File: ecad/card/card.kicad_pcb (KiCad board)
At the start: 4 copper layers, 133.4 x 32.2 mm, 136 parts, among them J1 Conn_01x03_Pin, J2 USB4105-GF-A, J3 10145226-0241N13LF, J4 Conn_01x03_Pin, J5 Conn_01x03_Pin, SW1 SW_Push, SW2 SW_Push, U1 W25Q128JVS, U2 RP2350_80QFN, U3 MCP23017_SO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

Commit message: current production try
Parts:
- SW1, SW2: footprint Button_Switch_SMD:SW_Push_1P1T_NO_Vertical_Wuerth_434133025816 -> Library:SW_TS-1088-AR02016
- turned SW1 to 180 degrees
- turned SW2 to 180 degrees
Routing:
- net /~{USB_BOOT}: track 7.50 -> 2.23 mm
- net GND: track 212.7 -> 207.6 mm, vias 52 -> 51
- net Net-(R1-Pad2): track 5.62 -> 1.90 mm
- net /~{RESET}: track 127.2 -> 128.4 mm

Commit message: revisions after feedback
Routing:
- net GND: track 207.6 -> 208.3 mm

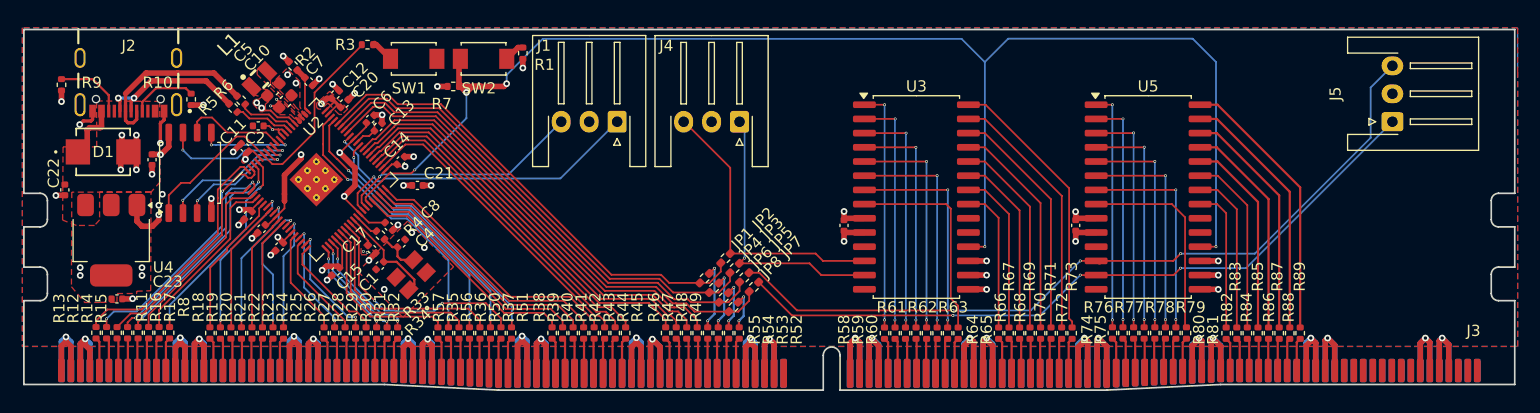
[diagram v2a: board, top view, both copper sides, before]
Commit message: various production cost changes
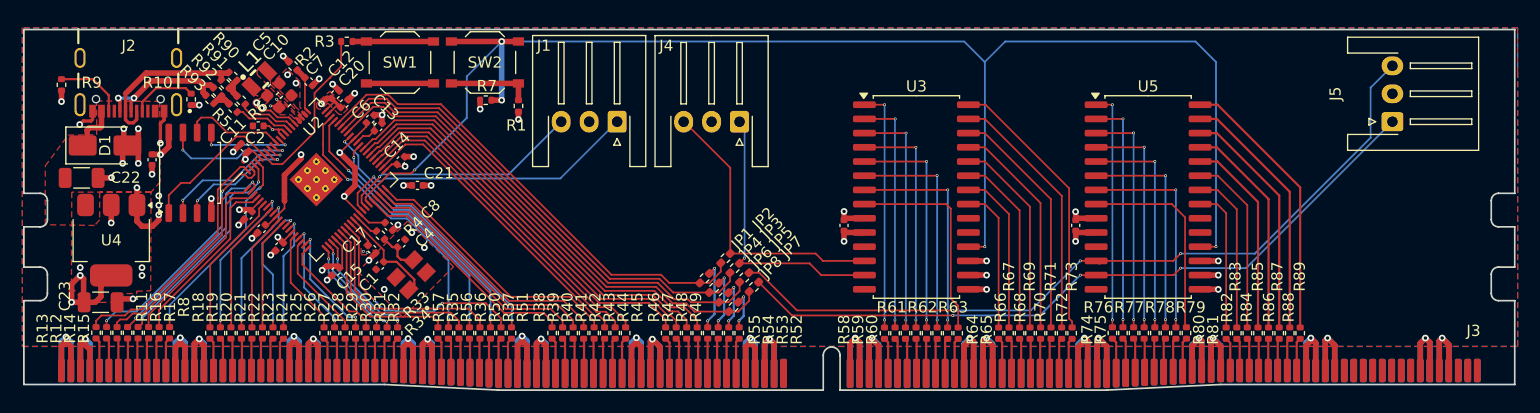
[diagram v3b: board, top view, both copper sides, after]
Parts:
- added R90: 10, Resistor_SMD:R_0402_1005Metric, F.Cu at (68.8, 53.4)
- added R91: 10, Resistor_SMD:R_0402_1005Metric, F.Cu at (68.2, 54.0)
- added R92: 10, Resistor_SMD:R_0402_1005Metric, F.Cu at (67.5, 54.7)
- added R93: 10, Resistor_SMD:R_0402_1005Metric, F.Cu at (66.8, 55.4)
- C22, C23: value 10u -> 22u; footprint Capacitor_SMD:C_0402_1005Metric -> Capacitor_SMD:C_1206_3216Metric
- D1: value D_Schottky -> SS34; footprint Library:DO-214BA_MCH-M -> Diode_SMD:D_SMA
- JP2, JP3, JP5, JP7: value Jumper_2_Small_Bridged -> 0402WGF0000TCE
- R5, R6: value 27 -> 22
- SW1, SW2: footprint Library:SW_TS-1088-AR02016 -> Button_Switch_SMD:SW_Push_1P1T_XKB_TS-1187A
- U4: value NCP1117-3.3_SOT223 -> AMS1117-3.3
- moved R1 4.73 mm to (94.4, 56.0)
- moved R7 3.16 mm to (91.5, 55.5)
- moved R3 1.87 mm to (79.0, 50.2)
- moved C22 1.85 mm to (55.3, 62.4), turned to 0 degrees
- moved C23 1.49 mm to (57.0, 73.5)
- moved SW1 1.27 mm to (83.8, 52.1)
- moved D1 0.60 mm to (57.4, 59.5)
- moved SW2 0.35 mm to (91.4, 52.1)
- turned R6 to -45 degrees
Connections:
- R5 pad 2: /USB_D+ -> Net-(R5-Pad2)
- R6 pad 1: Net-(U2-USB_DM) -> Net-(R6-Pad1)
- R6 pad 2: /USB_D- -> Net-(U2-USB_DM)
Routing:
- net 3.3V: track 215.7 -> 227.5 mm, vias 39 -> 41
- net GND: track 208.3 -> 215.7 mm, vias 51 -> 52
- net /~{RESET}: track 128.4 -> 135.1 mm
- net Net-(R1-Pad2): track 1.90 -> 7.50 mm
- net /~{USB_BOOT}: track 2.23 -> 7.24 mm
- net Net-(R6-Pad1): track 0.00 -> 3.68 mm
- net Net-(R5-Pad2): track 0.00 -> 3.59 mm
- net /USB_D-: track 16.0 -> 14.9 mm
- net /USB_D+: track 13.9 -> 12.9 mm

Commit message: ecad no weird resistor group
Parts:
- removed R90, R91, R92, R93: 10, Resistor_SMD:R_0402_1005Metric
- R5, R6: value 22 -> 27; footprint Resistor_SMD:R_0402_1005Metric -> Capacitor_SMD:C_0603_1608Metric_Pad1.08x0.95mm_HandSolder
- moved R5 0.52 mm to (68.5, 56.5)
- moved C2 0.05 mm to (71.2, 57.8)
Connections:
- R5 pad 2: Net-(R5-Pad2) -> /USB_D+
- R6 pad 1: Net-(R6-Pad1) -> /USB_D-
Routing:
- net Net-(R6-Pad1): track 3.68 -> 0.00 mm
- net Net-(R5-Pad2): track 3.59 -> 0.00 mm
- net /USB_D+: track 12.9 -> 13.7 mm
- net GND: track 215.7 -> 216.5 mm, vias 52 -> 53
- net /USB_D-: track 14.9 -> 15.6 mm

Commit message: stackup changes, prodction
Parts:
- SW1, SW2: value SW_Push -> TS-1187A-B-A-B
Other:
- board text added: "USB"
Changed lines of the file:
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@@
 			(layer "F.Mask"
 				(type "Top Solder Mask")
-				(color "Black")
+				(color "Green")
 				(thickness 0.01)
 				(material "Liquid Ink")
@@
 			(layer "B.Mask"
 				(type "Bottom Solder Mask")
-				(color "Black")
+				(color "Green")
 				(thickness 0.035)
 				(material "Liquid Ink")
@@
 			)
 		)
-		(property "Value" "SW_Push"
+		(property "Value" "TS-1187A-B-A-B"
 			(at 0 3.75 180)
 			(layer "F.Fab")
@@
 		(sheetname "Root")
 		(sheetfile "card.kicad_sch")
-		(attr smd)
+		(attr smd dnp)
 		(fp_line
 			(start -0.146267 0.51)
@@
 		(tags "resistor")
 		(property "Reference" "R7"
-			(at -0.1 1.275 360)
+			(at -0.1 1.275 0)
 			(layer "F.SilkS")
 			(effects
@@
 		)
 		(property "Value" "100k"
-			(at 0 1.17 360)
+			(at 0 1.17 0)
 			(layer "F.Fab")
 			(effects
@@
 		)
 		(fp_text user "${REFERENCE}"
-			(at 0 0 360)
+			(at 0 0 0)
 			(layer "F.Fab")
 			(effects
@@
 		(sheetname "Root")
 		(sheetfile "card.kicad_sch")
-		(attr smd)
+		(attr smd dnp)
 		(fp_line
 			(start -0.146267 -0.51)
@@
 			)
 		)
-		(property "Value" "SW_Push"
+		(property "Value" "TS-1187A-B-A-B"
 			(at 0 3.75 180)
 			(layer "F.Fab")
@@
 		(sheetname "Root")
 		(sheetfile "card.kicad_sch")
-		(attr smd)
+		(attr smd dnp)
 		(fp_line
 			(start 4.47 2.6)
@@
 		)
 	)
-	(gr_text "I2C 0\nUART 0"
+	(gr_text "USB"
 		(at 59.5 50 0)
 		(layer "B.SilkS" knockout)

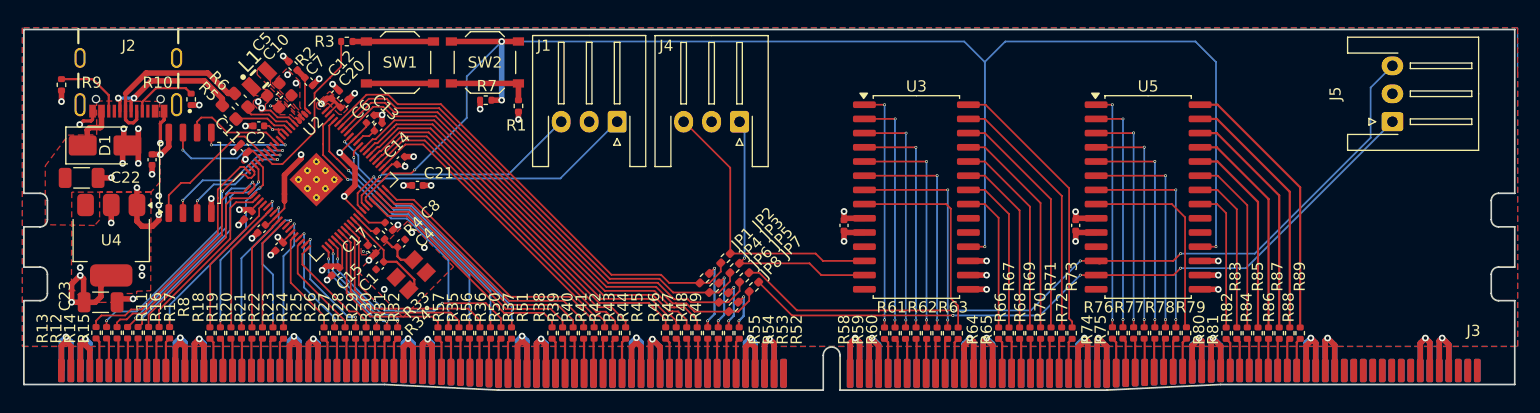
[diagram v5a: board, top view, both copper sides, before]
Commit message: double up for HASL
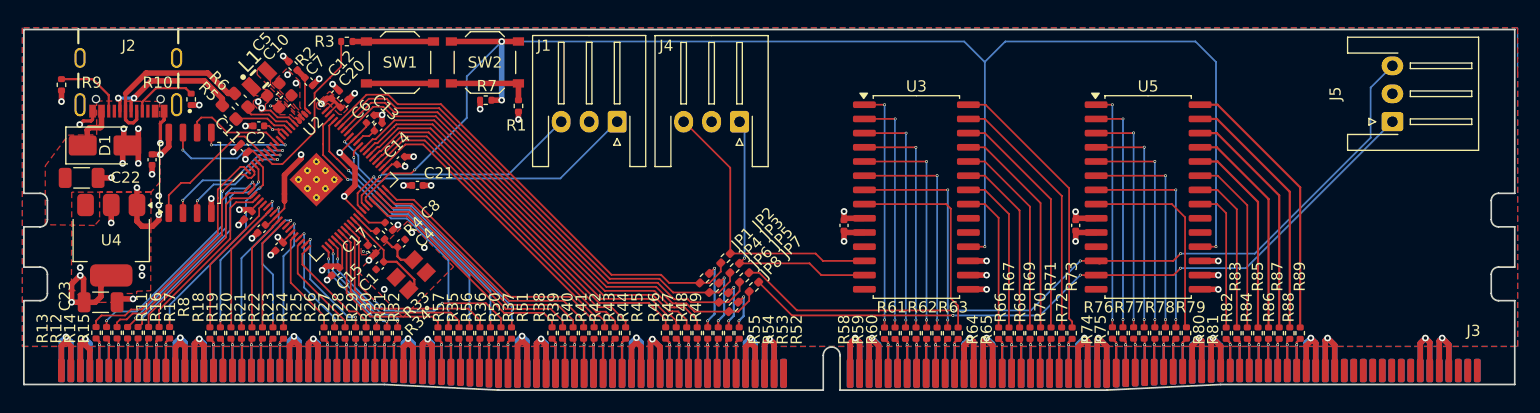
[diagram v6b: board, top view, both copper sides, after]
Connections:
- J3 pad 149: unconnected-(J3-Pad149) -> BUS05
- J3 pad 150: unconnected-(J3-Pad150) -> BUS06
- J3 pad 151: unconnected-(J3-Pad151) -> BUS07
- J3 pad 152: unconnected-(J3-Pad152) -> BUS08
- J3 pad 153: unconnected-(J3-Pad153) -> BUS09
- J3 pad 154: unconnected-(J3-Pad154) -> BUS10
- J3 pad 155: unconnected-(J3-Pad155) -> BUS11
- J3 pad 156: unconnected-(J3-Pad156) -> BUS12
- J3 pad 161: unconnected-(J3-Pad161) -> BUS17
- J3 pad 162: unconnected-(J3-Pad162) -> BUS18
- J3 pad 163: unconnected-(J3-Pad163) -> BUS19
- J3 pad 164: unconnected-(J3-Pad164) -> BUS20
- J3 pad 165: unconnected-(J3-Pad165) -> BUS21
- J3 pad 166: unconnected-(J3-Pad166) -> BUS22
- J3 pad 167: unconnected-(J3-Pad167) -> BUS23
- J3 pad 168: unconnected-(J3-Pad168) -> BUS24
- J3 pad 173: unconnected-(J3-Pad173) -> BUS29
- J3 pad 174: unconnected-(J3-Pad174) -> BUS30
- J3 pad 175: unconnected-(J3-Pad175) -> BUS31
- J3 pad 176: unconnected-(J3-Pad176) -> BUS32
- J3 pad 177: unconnected-(J3-Pad177) -> BUS33
- J3 pad 178: unconnected-(J3-Pad178) -> BUS34
- J3 pad 179: unconnected-(J3-Pad179) -> BUS35
- J3 pad 180: unconnected-(J3-Pad180) -> BUS36
- J3 pad 185: unconnected-(J3-Pad185) -> BUS41
- J3 pad 186: unconnected-(J3-Pad186) -> BUS42
- J3 pad 187: unconnected-(J3-Pad187) -> BUS43
- J3 pad 188: unconnected-(J3-Pad188) -> BUS44
- J3 pad 189: unconnected-(J3-Pad189) -> BUS45
- J3 pad 190: unconnected-(J3-Pad190) -> BUS46
- J3 pad 191: unconnected-(J3-Pad191) -> BUS47
- J3 pad 192: unconnected-(J3-Pad192) -> BUS48
- J3 pad 197: unconnected-(J3-Pad197) -> BUS53
- J3 pad 198: unconnected-(J3-Pad198) -> BUS54
- J3 pad 199: unconnected-(J3-Pad199) -> BUS55
- J3 pad 200: unconnected-(J3-Pad200) -> BUS56
- J3 pad 201: unconnected-(J3-Pad201) -> BUS57
- J3 pad 202: unconnected-(J3-Pad202) -> BUS58
- J3 pad 203: unconnected-(J3-Pad203) -> BUS59
- J3 pad 204: unconnected-(J3-Pad204) -> BUS60
- J3 pad 209: unconnected-(J3-Pad209) -> BUS65
- J3 pad 210: unconnected-(J3-Pad210) -> BUS66
- J3 pad 211: unconnected-(J3-Pad211) -> BUS67
- J3 pad 212: unconnected-(J3-Pad212) -> BUS68
- J3 pad 213: unconnected-(J3-Pad213) -> BUS69
- J3 pad 214: unconnected-(J3-Pad214) -> BUS70
- J3 pad 215: unconnected-(J3-Pad215) -> BUS71
- J3 pad 216: unconnected-(J3-Pad216) -> BUS72
- J3 pad 226: unconnected-(J3-Pad226) -> BEX082
- J3 pad 227: unconnected-(J3-Pad227) -> BEX083
- J3 pad 228: unconnected-(J3-Pad228) -> BEX084
- J3 pad 229: unconnected-(J3-Pad229) -> BEX085
- J3 pad 230: unconnected-(J3-Pad230) -> BEX086
- J3 pad 231: unconnected-(J3-Pad231) -> BEX087
- J3 pad 232: unconnected-(J3-Pad232) -> BEX088
- J3 pad 233: unconnected-(J3-Pad233) -> BEX089
- J3 pad 238: unconnected-(J3-Pad238) -> BEX094
- J3 pad 239: unconnected-(J3-Pad239) -> BEX095
- J3 pad 240: unconnected-(J3-Pad240) -> BEX096
- J3 pad 241: unconnected-(J3-Pad241) -> BEX097
- J3 pad 242: unconnected-(J3-Pad242) -> BEX098
- J3 pad 243: unconnected-(J3-Pad243) -> BEX099
- J3 pad 244: unconnected-(J3-Pad244) -> BEX100
- J3 pad 245: unconnected-(J3-Pad245) -> BEX101
- J3 pad 250: unconnected-(J3-Pad250) -> BEX106
- J3 pad 251: unconnected-(J3-Pad251) -> BEX107
- J3 pad 252: unconnected-(J3-Pad252) -> BEX108
- J3 pad 253: unconnected-(J3-Pad253) -> BEX109
- J3 pad 254: unconnected-(J3-Pad254) -> BEX110
- J3 pad 255: unconnected-(J3-Pad255) -> BEX111
- J3 pad 256: unconnected-(J3-Pad256) -> BEX112
- J3 pad 257: unconnected-(J3-Pad257) -> BEX113
- J3 pad 262: unconnected-(J3-Pad262) -> BEX118
- J3 pad 263: unconnected-(J3-Pad263) -> BEX119
- J3 pad 264: unconnected-(J3-Pad264) -> BEX120
- J3 pad 265: unconnected-(J3-Pad265) -> BEX121
- J3 pad 266: unconnected-(J3-Pad266) -> BEX122
- J3 pad 267: unconnected-(J3-Pad267) -> BEX123
- J3 pad 268: unconnected-(J3-Pad268) -> BEX124
- J3 pad 269: unconnected-(J3-Pad269) -> BEX125
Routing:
- net BUS44: track 3.12 -> 5.67 mm, vias 0 -> 1
- net BUS70: track 3.14 -> 5.69 mm, vias 0 -> 1
- net BUS55: track 3.15 -> 5.70 mm, vias 0 -> 1
- net BUS46: track 3.15 -> 5.70 mm, vias 0 -> 1
- net BEX113: track 3.24 -> 5.79 mm, vias 0 -> 1
- net BEX112: track 3.19 -> 5.75 mm, vias 0 -> 1
- net BEX107: track 3.20 -> 5.75 mm, vias 0 -> 1
- net BEX106: track 3.24 -> 5.79 mm, vias 0 -> 1
- net BEX100: track 3.17 -> 5.73 mm, vias 0 -> 1
- net BEX096: track 3.14 -> 5.69 mm, vias 0 -> 1
- net BEX095: track 3.18 -> 5.73 mm, vias 0 -> 1
- net BEX087: track 3.13 -> 5.69 mm, vias 0 -> 1
- net BUS72: track 3.21 -> 5.77 mm, vias 0 -> 1
- net BUS71: track 3.17 -> 5.73 mm, vias 0 -> 1
- net BUS69: track 3.10 -> 5.66 mm, vias 0 -> 1
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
